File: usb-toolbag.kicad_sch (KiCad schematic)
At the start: 29 parts, among them J1 USB_A, J2 Conn_01x25_Pin, SW1 KMR2, SW2 KMR2, U1 29F32G08-TSOP48, U2 RT9080-3.3, U3 RP2040, U4 8MB QSPI, Y1 12MHz/12pF

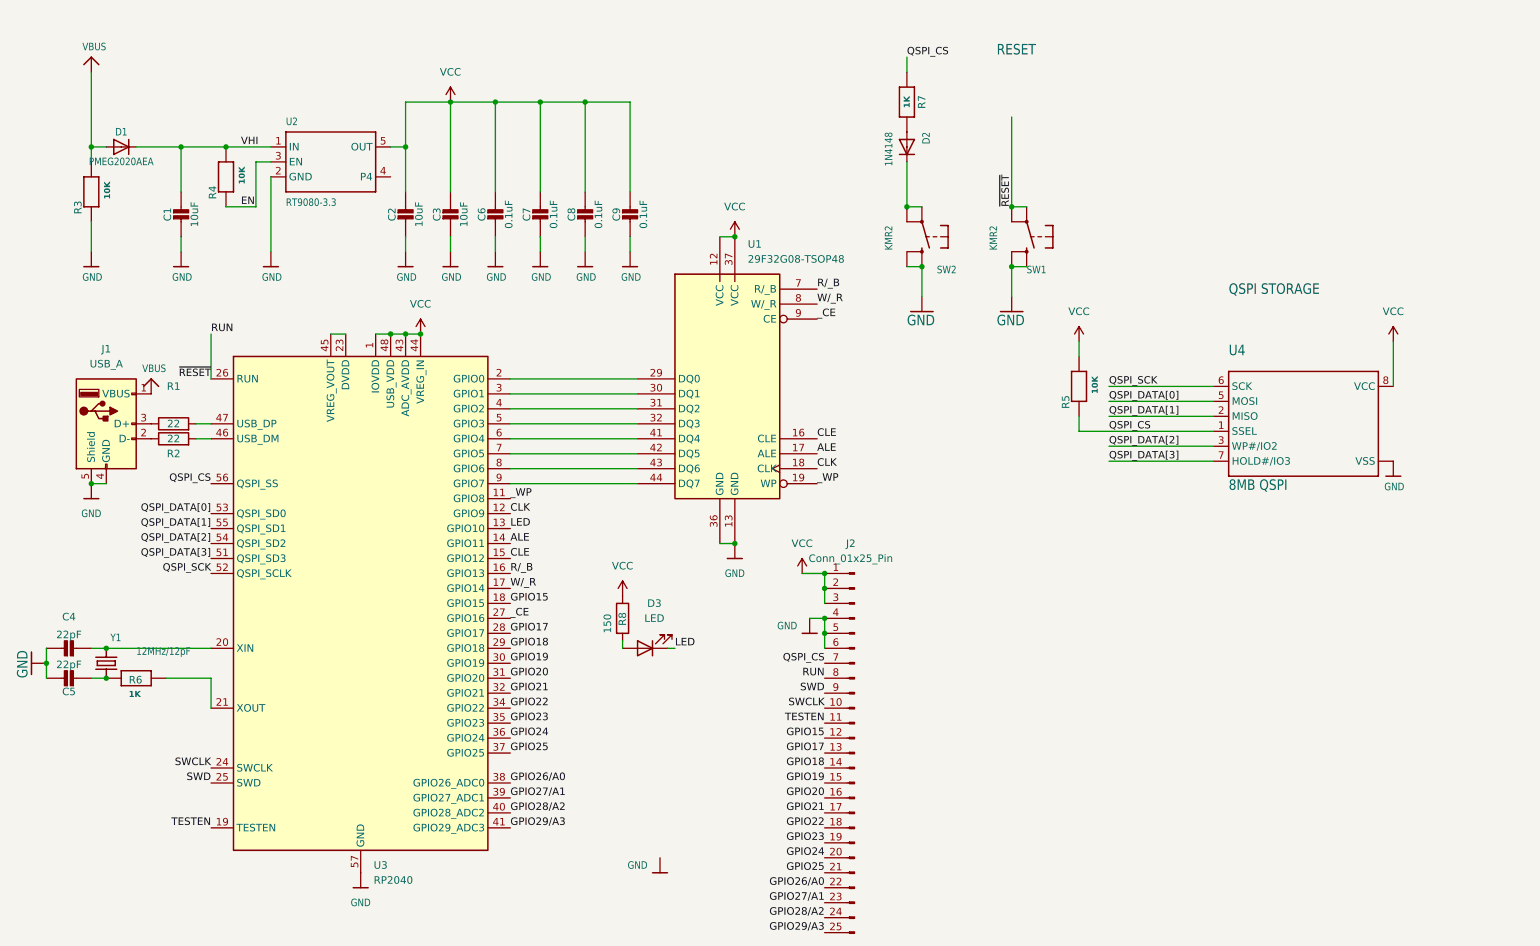
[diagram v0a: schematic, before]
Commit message: Update schematic
Tweaked and cleaned up schematic.
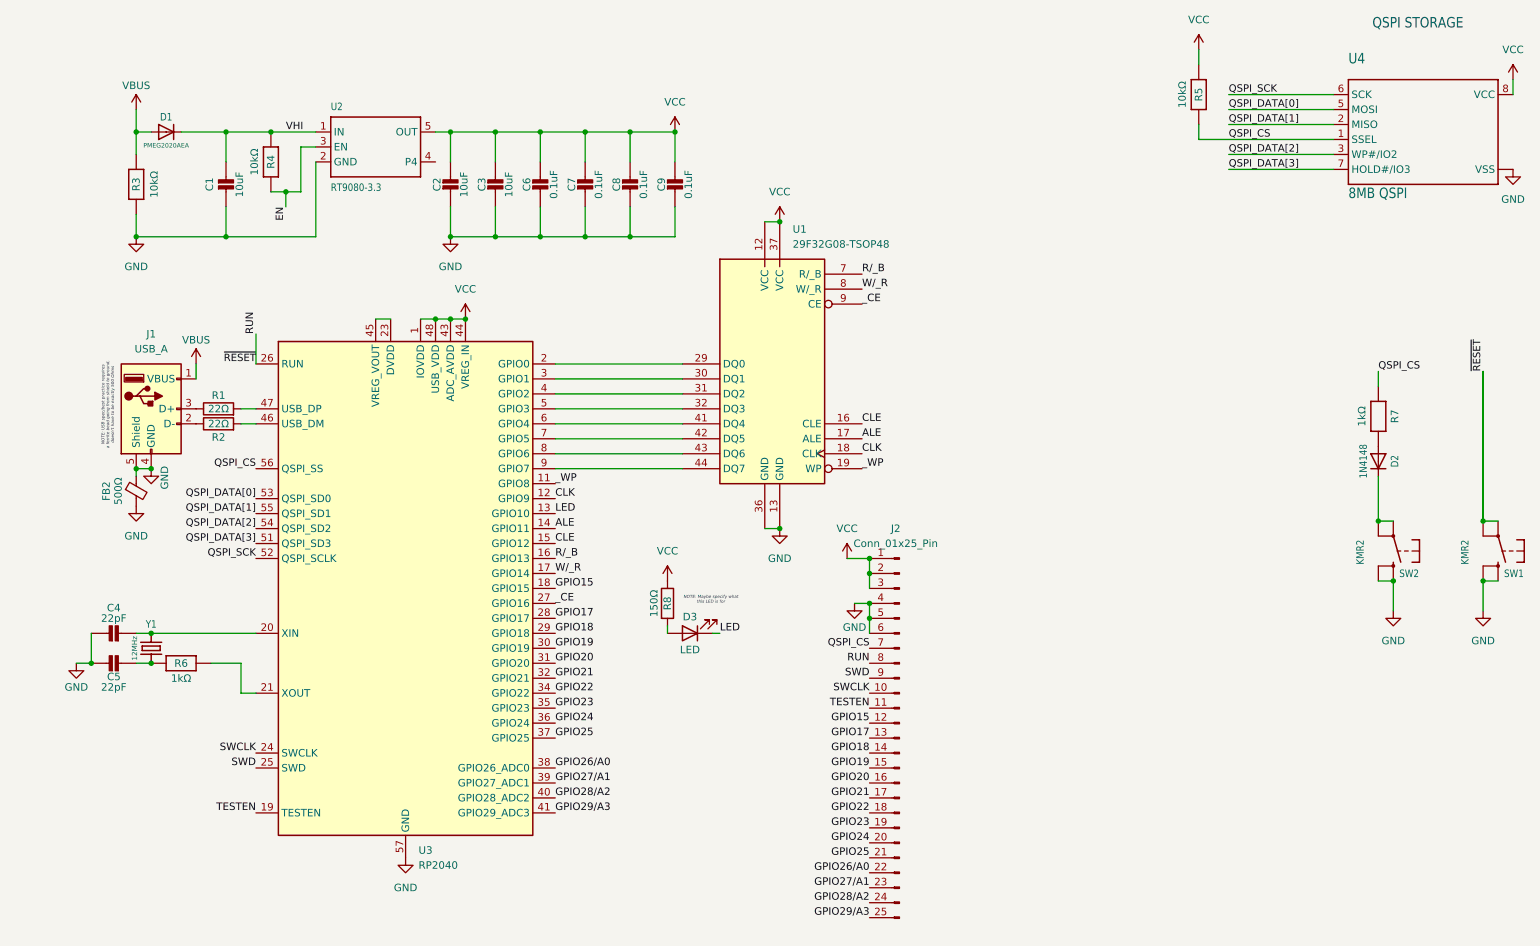
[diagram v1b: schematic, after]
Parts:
- added FB2: 500Ω, symbol Device:FerriteBead_Small
- R1, R2: value 22 -> 22Ω
- R3, R4, R5: value 10K -> 10kΩ
- R6, R7: value 1K -> 1kΩ
- R8: value 150 -> 150Ω
- Y1: value 12MHz/12pF -> 12MHz
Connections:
- net GND: now also FB2.1, FB2.2
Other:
- note added: "NOTE: Maybe specify what this LED is for"
- note added: "NOTE: USB spec/best practice requires a ferrite bead going from shield to ground, doesn't have to be exactly 500 Ohms"
- note removed: "RESET"
- moved on the sheet: C1, C2, C3, C4, C5, C6, C7, C8, C9, D1, D2, D3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
